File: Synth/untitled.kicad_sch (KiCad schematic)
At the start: 9 parts, among them U1 Opamp_Dual

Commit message: almost done w layoutgit add *
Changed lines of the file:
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@@
   (junction (at 162.814 86.868) (diameter 0) (color 0 0 0 0)
+  )
+  (junction (at 204.089 87.884) (diameter 0) (color 0 0 0 0)
   )
   (junction (at 162.941 86.868) (diameter 0) (color 0 0 0 0)
@@
     (stroke (width 0) (type default))
   )
+  (wire (pts (xy 205.613 87.884) (xy 204.089 87.884))
+    (stroke (width 0) (type default))
+  )
   (wire (pts (xy 107.315 122.682) (xy 110.871 122.682))
     (stroke (width 0) (type default))
@@
     (stroke (width 0) (type default))
   )
-  (wire (pts (xy 204.089 87.757) (xy 204.089 90.297))
+  (wire (pts (xy 204.089 87.757) (xy 204.089 87.884))
     (stroke (width 0) (type default))
   )
@@
     (stroke (width 0) (type default))
   )
+  (wire (pts (xy 204.089 87.884) (xy 204.089 90.297))
+    (stroke (width 0) (type default))
+  )
   (wire (pts (xy 72.136 122.682) (xy 72.136 120.142))
     (stroke (width 0) (type default))
@@
     (fill (type none))
   )
-  (rectangle (start 130.429 75.438) (end 217.043 105.791)
+  (rectangle (start 130.429 75.438) (end 219.964 105.791)
     (stroke (width 0) (type default))
     (fill (type none))
@@
     )
   )
-  (global_label "Filter Out" (shape input) (at 204.089 87.884 0) (fields_autoplaced)
+  (global_label "Filter Out" (shape input) (at 205.613 87.884 0) (fields_autoplaced)
     (effects (font (size 1.27 1.27)) (justify left))
-    (property "Intersheetrefs" "${INTERSHEET_REFS}" (at 216.2061 87.884 0)
+    (property "Intersheetrefs" "${INTERSHEET_REFS}" (at 217.7301 87.884 0)
       (effects (font (size 1.27 1.27)) (justify left) hide)
     )

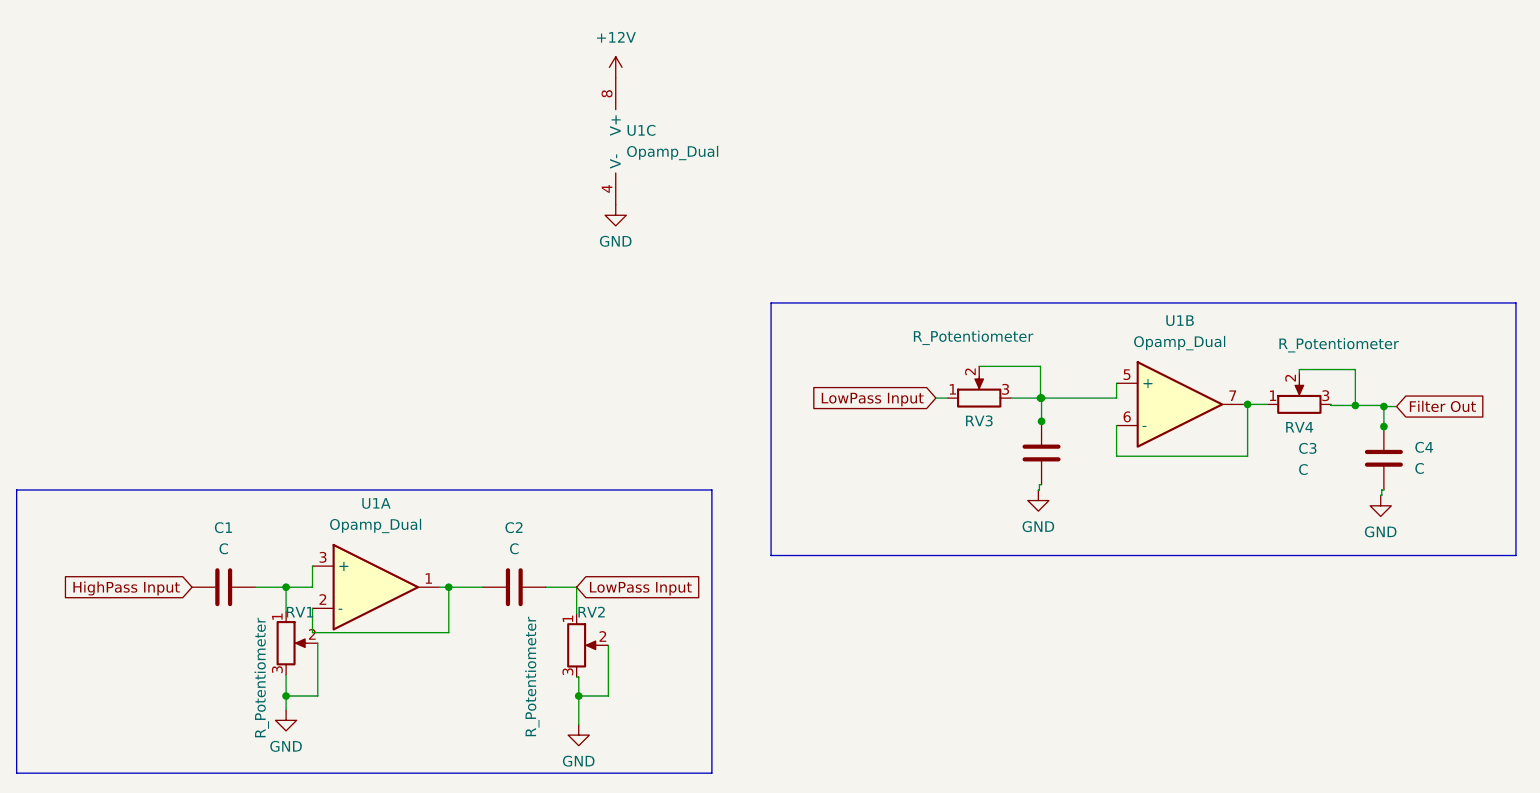
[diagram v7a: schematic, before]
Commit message: changed hierarchical labels
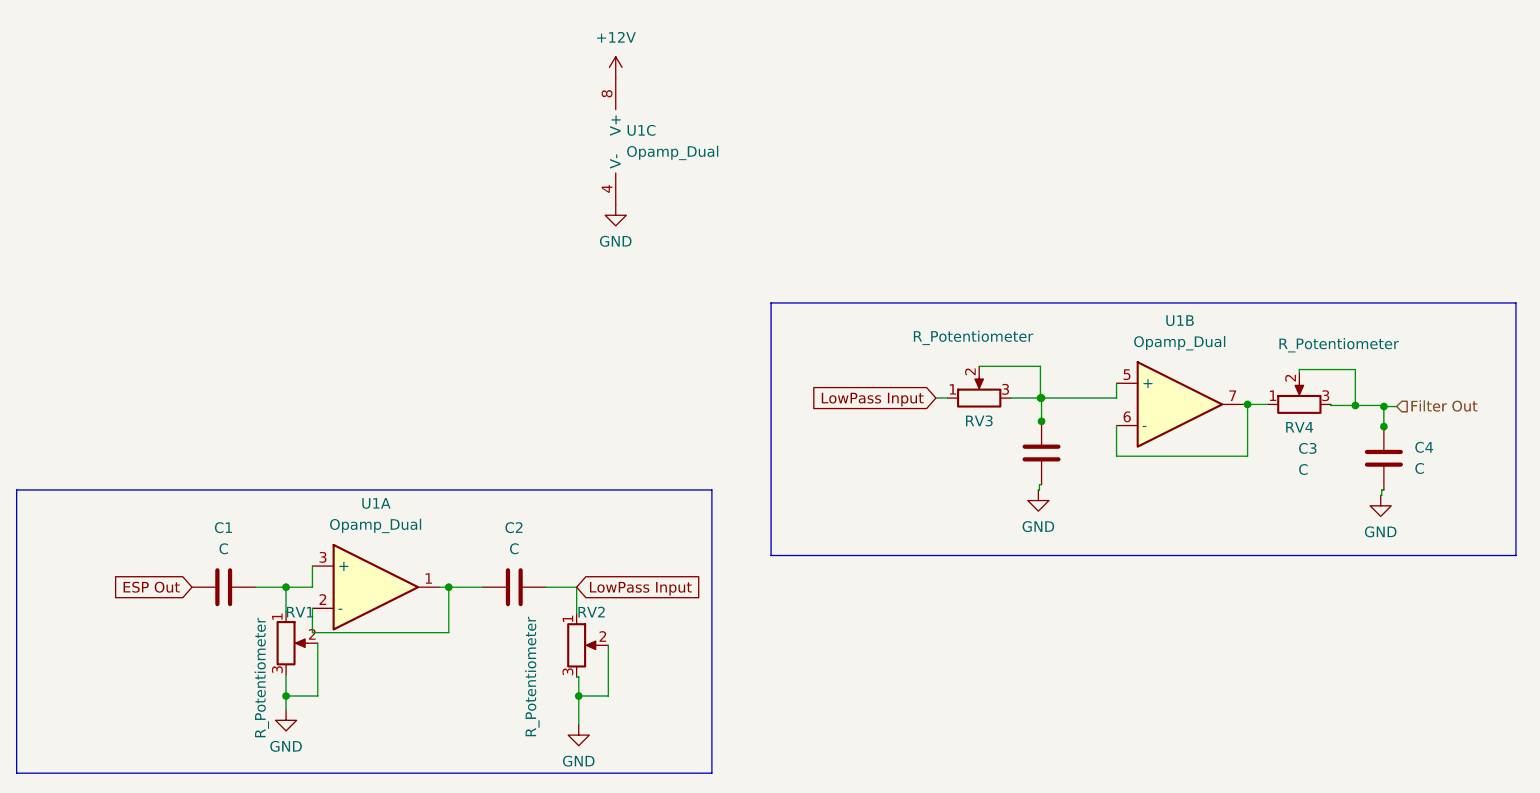
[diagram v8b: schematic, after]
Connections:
- net HighPass Input renamed ESP Out
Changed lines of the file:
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@@
     (fill (type none))
+  )
+  (global_label "ESP Out" (shape input) (at 60.833 109.601 180) (fields_autoplaced)
+    (effects (font (size 1.27 1.27)) (justify right))
+    (property "Intersheetrefs" "${INTERSHEET_REFS}" (at 50.0465 109.601 0)
+      (effects (font (size 1.27 1.27)) (justify right) hide)
+    )
   )
   (global_label "LowPass Input" (shape input) (at 107.061 109.601 0) (fields_autoplaced)
@@
     )
   )
-  (global_label "Filter Out" (shape input) (at 205.613 87.884 0) (fields_autoplaced)
+  (hierarchical_label "Filter Out" (shape input) (at 205.613 87.884 0) (fields_autoplaced)
     (effects (font (size 1.27 1.27)) (justify left))
-    (property "Intersheetrefs" "${INTERSHEET_REFS}" (at 217.7301 87.884 0)
-      (effects (font (size 1.27 1.27)) (justify left) hide)
-    )
-  )
-  (global_label "HighPass Input" (shape input) (at 60.833 109.601 180) (fields_autoplaced)
-    (effects (font (size 1.27 1.27)) (justify right))
-    (property "Intersheetrefs" "${INTERSHEET_REFS}" (at 43.3942 109.601 0)
-      (effects (font (size 1.27 1.27)) (justify right) hide)
-    )
   )
   (symbol (lib_id "Device:R_Potentiometer") (at 72.136 116.332 0) (unit 1)
